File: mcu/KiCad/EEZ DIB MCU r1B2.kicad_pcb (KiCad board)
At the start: 4 copper layers, 139 x 70 mm, 193 parts, among them IC1 TPD4E001DRLR, IC10 TPS2051BDBVR, IC11 TPS61169DCKR, IC12 TPD4E001DRLR, IC13 TPA6205A1DGN, IC14 TPD4E001DRLR, IC15 AR1021-I/SS, IC16 TPD4E001DRLR, IC17 DP83848CVV_NOPB, IC2 SN74LVC2G34DBVR, IC3 BTS3408G, IC4 STM32F769IGT6, IC5 LD1117ADT33TR, IC6 TPD4E001DRLR, IC7 TPD4E001DRLR, IC8 IS42S16400J, IC9 BR24G64FVT-3AGE2, J1 503398-1892, J2 67803-8020, Q1 MMBT5551, SW1 PEC16-2215F-S0024, SW2 B3F-3152, X1 ZL263-40DG, X2 ZL231-16KG, X3 1844249, X4 ZL231-20KG, X5 LMJTAB881243M-L, Y1 10MHz

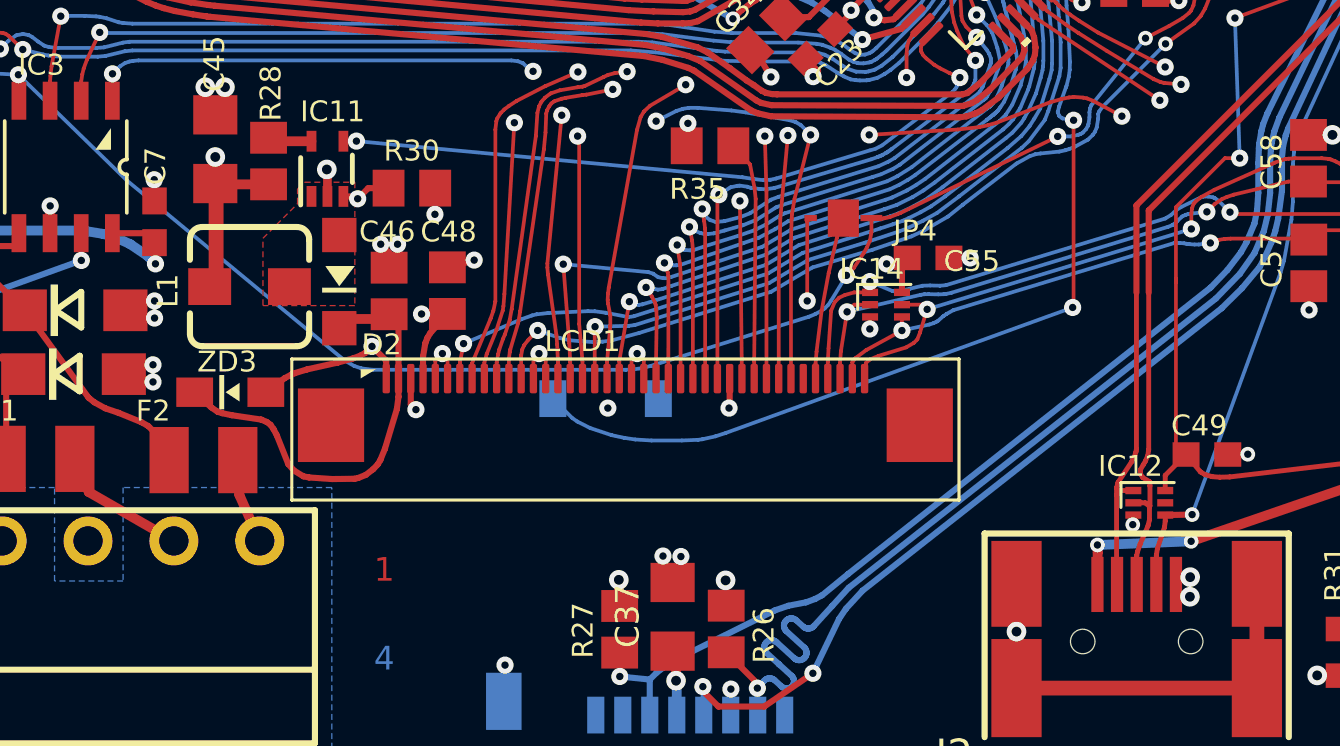
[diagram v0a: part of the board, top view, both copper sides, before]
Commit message: Left PE Ground trace dangling on USB connector
Connected PE Trace, and 5V to L1,
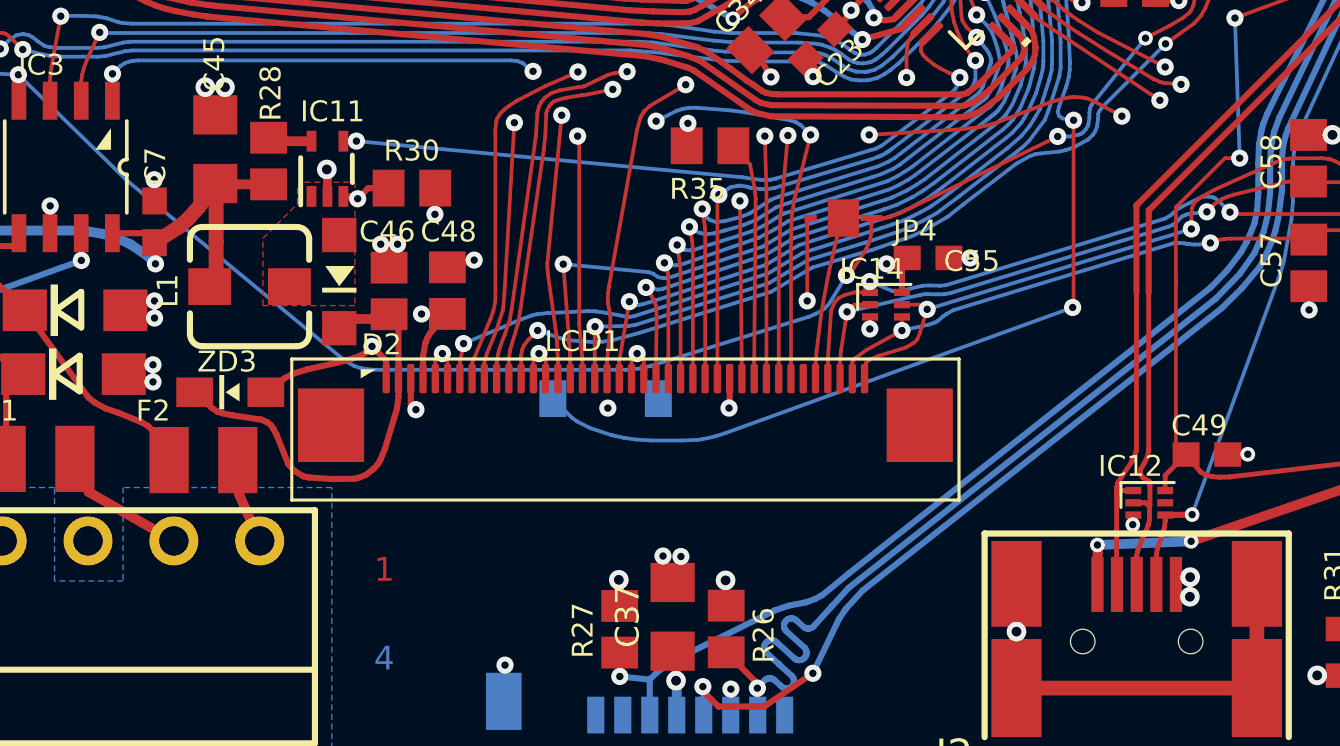
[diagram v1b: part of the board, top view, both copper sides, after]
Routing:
- net PE: track 176.2 -> 173.1 mm
- net +5V: track 172.9 -> 175.3 mm, vias 7 -> 6
- net GND: track 160.7 -> 162.2 mm
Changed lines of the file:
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@@
     (thickness 1.6)
     (drawings 101)
-    (tracks 9814)
+    (tracks 9819)
     (zones 0)
     (modules 193)
@@
   )
   (setup
-    (last_trace_width 0.2)
+    (last_trace_width 0.6)
     (user_trace_width 0.15)
     (user_trace_width 0.25)
@@
   (via (at 164.53 127.47) (size 0.6) (drill 0.3) (layers Top Bottom) (net 4))
   (segment (start 164.53 127.47) (end 163.7134 127.4814) (width 0.25) (layer Top) (net 4))
+  (segment (start 162.18 132.48) (end 162.17 133.28) (width 0.2) (layer Top) (net 4))
+  (segment (start 162.18 132.48) (end 161.6011 132.7786) (width 0.2) (layer Top) (net 4))
   (via (at 103.275 103.2752) (size 0.7) (drill 0.3) (layers Top Bottom) (net 5))
   (segment (start 86.2443 91.1365) (end 88.2001 91.1365) (width 0.25) (layer Top) (net 5) (status 30))
@@
   (segment (start 181.4435 89.8386) (end 202.38 89.8386) (width 0.1524) (layer Bottom) (net 6))
   (via (at 82.0011 136.5036) (size 5.5) (drill 3.2) (layers Top Bottom) (net 7))
-  (via (at 122.4393 115.3529) (size 0.8) (drill 0.4) (layers Top Bottom) (net 8))
   (segment (start 124.611 116.468) (end 122.4719 116.468) (width 0.4) (layer Top) (net 8) (status 30))
   (segment (start 122.4719 116.468) (end 122.4393 116.4354) (width 0.4) (layer Top) (net 8) (status 30))
-  (segment (start 122.4393 115.3529) (end 122.4393 116.4354) (width 0.4) (layer Top) (net 8) (status 20))
-  (segment (start 122.4719 116.468) (end 122.4719 120.3745) (width 0.6096) (layer Top) (net 8) (status 30))
   (segment (start 122.4719 120.3745) (end 122.2103 120.6361) (width 0.6096) (layer Top) (net 8) (status 30))
   (via (at 171.9693 137.6922) (size 0.7) (drill 0.3) (layers Top Bottom) (net 8))
@@
   (segment (start 82.256715 85.12) (end 82.178423 85.24) (width 0.4) (layer Power) (net 8))
   (segment (start 86.17 81.1372) (end 82.68 84.6272) (width 0.4) (layer Power) (net 8))
+  (segment (start 122.4719 116.468) (end 122.4719 118.81) (width 0.6096) (layer Top) (net 8))
+  (segment (start 122.4719 118.81) (end 122.4719 120.3745) (width 0.6096) (layer Top) (net 8))
+  (segment (start 119.9628 118.8445) (end 120.93 118.222334) (width 0.6) (layer Top) (net 8))
+  (segment (start 121.79203 117.36) (end 121.34 117.871246) (width 0.6) (layer Top) (net 8))
+  (segment (start 121.34 117.871246) (end 120.93 118.222334) (width 0.6) (layer Top) (net 8))
+  (segment (start 121.79203 117.36) (end 122.4393 116.4354) (width 0.6) (layer Top) (net 8))
   (via (at 162.838 78.8023) (size 0.7) (drill 0.3) (layers Top Bottom) (net 9))
   (via (at 162.6856 73.227) (size 0.7) (drill 0.3) (layers Top Bottom) (net 9))
@@
   (segment (start 80.720111 84.43) (end 80.350159 85.09) (width 0.6096) (layer Power) (net 29))
   (segment (start 81.0347 84.05) (end 80.720111 84.43) (width 0.6096) (layer Power) (net 29))
-  (segment (start 154.2081 131.65) (end 154.2081 129.9716) (width 0.6096) (layer Power) (net 29))
   (segment (start 89.62 138.48783) (end 90.02 138.667866) (width 0.6096) (layer Power) (net 29))
-  (segment (start 149.3265 138.11) (end 152.95 134.4865) (width 0.6096) (layer Power) (net 29))
   (segment (start 88.9597 138.02) (end 89.62 138.48783) (width 0.6096) (layer Power) (net 29))
   (segment (start 148.72 138.495843) (end 149.3265 138.11) (width 0.6096) (layer Power) (net 29))
   (segment (start 90.59 138.773659) (end 91.46 138.8479) (width 0.6096) (layer Power) (net 29))
   (segment (start 80.1991 127.7036) (end 80.1991 128.45) (width 0.6096) (layer Power) (net 29))
-  (segment (start 153.781926 133.42) (end 154.115345 132.51) (width 0.6096) (layer Power) (net 29))
   (segment (start 90.02 138.667866) (end 90.59 138.773659) (width 0.6096) (layer Power) (net 29))
   (segment (start 91.46 138.8479) (end 147.46 138.8479) (width 0.6096) (layer Power) (net 29))
   (segment (start 147.46 138.8479) (end 148.06 138.741414) (width 0.6096) (layer Power) (net 29))
   (segment (start 148.06 138.741414) (end 148.72 138.495843) (width 0.6096) (layer Power) (net 29))
-  (segment (start 152.95 134.4865) (end 153.781926 133.42) (width 0.6096) (layer Power) (net 29))
-  (segment (start 154.115345 132.51) (end 154.2081 131.65) (width 0.6096) (layer Power) (net 29))
   (segment (start 80.1991 128.45) (end 80.272866 128.82) (width 0.6096) (layer Power) (net 29))
   (segment (start 80.272866 128.82) (end 80.436645 129.21) (width 0.6096) (layer Power) (net 29))
@@
   (segment (start 155.1011 134.7) (end 155.1011 137.0036) (width 0.6) (layer Top) (net 29))
   (via (at 155.1011 134.7) (size 0.8) (drill 0.4) (layers Top Bottom) (net 29))
+  (segment (start 153.68 135.028168) (end 152.6 135.391479) (width 0.6096) (layer Power) (net 29))
+  (segment (start 153.68 135.028168) (end 155.1011 134.7) (width 0.6096) (layer Power) (net 29))
+  (segment (start 151.93 135.741895) (end 150.74 136.6965) (width 0.6096) (layer Power) (net 29))
+  (segment (start 149.3265 138.11) (end 150.74 136.6965) (width 0.6096) (layer Power) (net 29))
+  (segment (start 151.93 135.741895) (end 152.6 135.391479) (width 0.6096) (layer Power) (net 29))
   (segment (start 90.1686 97.6237) (end 90.1296 97.6237) (width 0.25) (layer Top) (net 30) (status 30))
   (segment (start 90.1296 97.6237) (end 90.1296 97.0386) (width 0.4) (layer Top) (net 30) (status 10))

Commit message: Refill Zones...
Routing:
- net PE: track 173.1 -> 188.6 mm
- net Net-(R55-Pad1): track 22.9 -> 27.7 mm

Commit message: Updating Kicad Files To Reflect Latest Commits
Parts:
- added TP1: PCB_TEST_TABSHIELD, EEZ DIB MCU r1B2:PCB_SHIELD_TAB, F.Cu at (183.2, 95.9)
- C37: value 10u -> 4u7
- D2: footprint EEZ DIB MCU r1B2:SOD123 -> EEZ DIB MCU r1B2:SOD323-R
- SW2: value B3F-3152 -> TL1100CF160Q; footprint EEZ DIB MCU r1B2:B3F-315X -> EEZ DIB MCU r1B2:TL1100C
- moved R27 7.88 mm to (146.8, 134.0), turned to 180 degrees
- moved C3 7.29 mm to (201.1, 130.5), turned to 0 degrees
- moved C37 4.18 mm to (139.4, 137.9), turned to 180 degrees
- moved R26 3.78 mm to (146.8, 136.0), turned to 180 degrees
- moved ZD3 3.05 mm to (125.9, 126.1), turned to 90 degrees
- moved B1 2.28 mm to (205.4, 125.7)
- moved SW2 2.24 mm to (210.5, 136.0), turned to 90 degrees
- moved RN1 2.12 mm to (104.9, 109.1)
- moved LCD1 1.52 mm to (140.7, 126.3)
- moved ZD2 0.12 mm to (116.6, 121.6)
- moved C70 0.11 mm to (104.9, 102.9)
- moved F2 0.11 mm to (122.0, 127.6)
- moved C21 0.11 mm to (167.1, 103.7)
- moved R7 0.07 mm to (110.5, 122.8)
- moved R3 0.07 mm to (107.5, 122.8)
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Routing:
- net /TFT, Audio, USB/VLED+: track 18.2 -> 14.1 mm
- net GND: track 162.2 -> 165.7 mm, vias 156 -> 155
- net Net-(JP6-Pad1): track 9.10 -> 11.9 mm
- net VDD: track 66.6 -> 69.2 mm
- net Net-(IC17-Pad2): track 3.22 -> 5.75 mm
- net Net-(IC17-Pad4): track 4.25 -> 6.43 mm
- net /Ethernet PHY/ETH_RX_CLK: track 45.2 -> 43.1 mm
- net /Ethernet PHY/ETH_RX_DV: track 38.2 -> 36.2 mm
- net /Ethernet PHY/MCLK_25: track 72.7 -> 70.6 mm
- net /Ethernet PHY/ETH_CRS: track 53.6 -> 55.6 mm
- net Net-(IC17-Pad40): track 4.21 -> 6.17 mm
- net Net-(IC17-Pad38): track 5.37 -> 7.22 mm
- net Net-(IC17-Pad41): track 5.56 -> 7.29 mm
- net /I/O connectors, encoders, user SW/USER_SW: track 92.4 -> 90.7 mm
- net Net-(IC17-Pad34): track 10.7 -> 12.3 mm
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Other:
- rule pad_to_mask_clearance: 0.1 -> 0.065
- board text added: "EEZ DIB MCU (10/2018 r1B2)"
- board text added: "GND-35"
- board text added: "OE_SYNC-39"
- board text added: "OUT_SER-37"
- board text added: "SPI2_CLK-9"
- board text added: "SPI2_CSA-15"
- board text added: "SPI2_CSB-17"
- board text added: "SPI2_IRQ-19"
- board text added: "SPI2_MISO-11"
- board text added: "SPI2_MOSI-13"
- board text added: "SPI5_CLK-23"
- board text added: "SPI5_CSA-29"
- board text added: "SPI5_CSB-31"
- board text added: "SPI5_IRQ-33"
- board text added: "SPI5_MISO-25"
- board text added: "SPI5_MOSI-27"
- board text removed: "EEZ DIB MCU (09/2018 r1B2)"
- board text removed: "GND-36"
- board text removed: "OE_SYNC"
- board text removed: "OUT_SER"
- board text removed: "SPI2_CLK"
- board text removed: "SPI2_CSA"
- board text removed: "SPI2_CSB"
- board text removed: "SPI2_IRQ"
- board text removed: "SPI2_MISO"
- board text removed: "SPI2_MOSI"
- board text removed: "SPI5_CLK"
- board text removed: "SPI5_CSA"
- board text removed: "SPI5_CSB"
- board text removed: "SPI5_IRQ"
- board text removed: "SPI5_MISO"
- board text removed: "SPI5_MOSI"
